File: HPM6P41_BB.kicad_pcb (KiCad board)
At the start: 4 copper layers, 152.8 x 80.3 mm, 287 parts, among them J1 USB_B, J10 Conn_01x01, J11 Conn_01x01, J12 Conn_01x01, J2 USB_C_Receptacle_USB2.0_16P, J3 Conn_02x16_Odd_Even, J4 Conn_ARM_JTAG_SWD_20, J5 Conn_01x03, J6 Conn_01x03, J7 SMA, J8 SMA, J9 Conn_01x01, Q1 HYG080N10LS1C2, Q2 HYG080N10LS1C2, Q3 HYG080N10LS1C2, Q4 HYG080N10LS1C2, Q5 S8050, SW1 焊盘, SW2 Push_Button, SW3 Push_Button, SW4 Push_Button, U1 UCC27211ADRMR, U10 TJA1044GTK/3Z, U11 TPS54302, U12 LP5907MFX-3.3, U13 REF3030, U14 LM5164DDA, U15 SY8089, U16 INA241A3xDDF, U17 INA241A3xDDF, U18 UCC27519, U19 XC6206PxxxMR, U2 UCC27211ADRMR, U20 SGM8551XN, U21 SGM8551XN, U22 TMP112xxDRL, U23 TPD4E05U06DQA, U3 UCC27519, U4 HPM6P41IPB1, U5 TPD4E05U06DQA, U6 AT24C08C-SSHM-T, U7 TMP112xxDRL, U8 TMP112xxDRL, U9 SIT3088ETK, Y1 24MHz ±10ppm 6pF

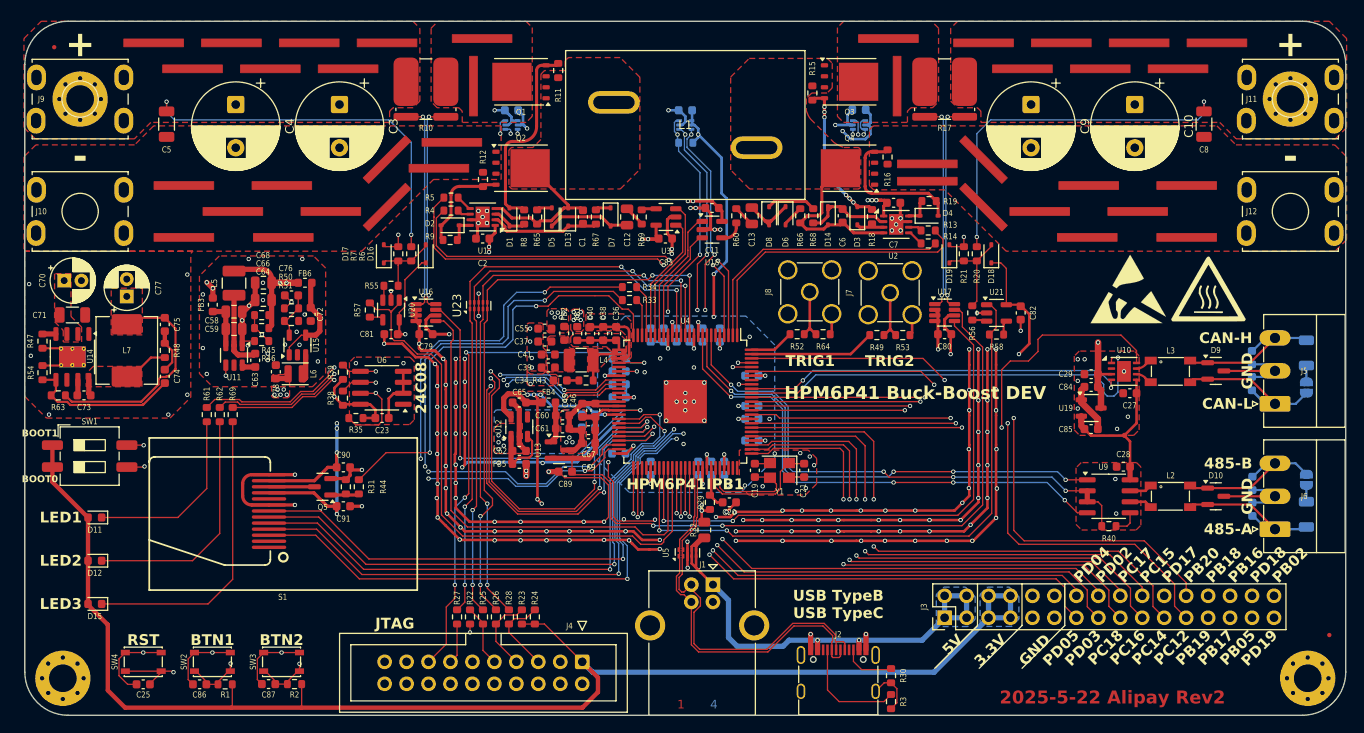
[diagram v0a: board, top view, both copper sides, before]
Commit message: 添加蜂鸣器IO及走线，更改PINMUX配图
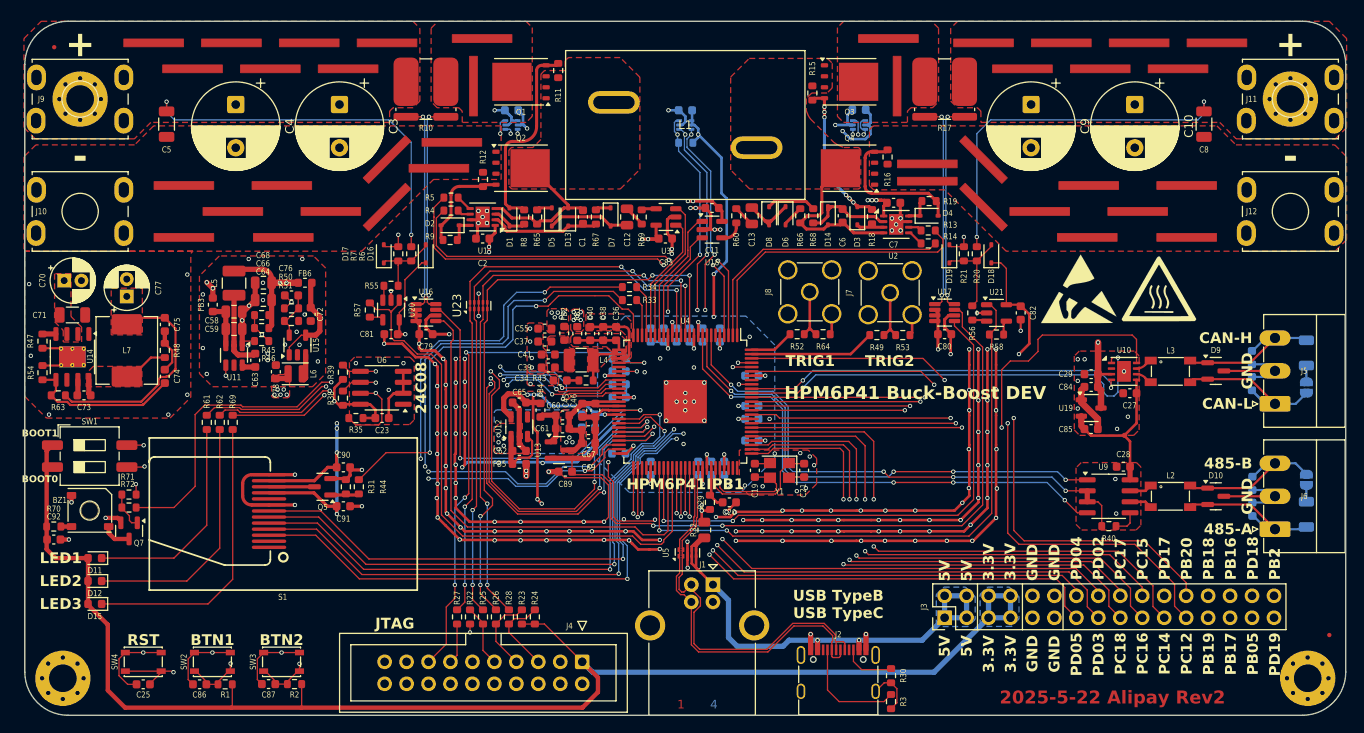
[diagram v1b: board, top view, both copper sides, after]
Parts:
- added BZ1: Buzzer_DummyPIn3, 1MyFootPrint:Buzzer_5020_MetalHole, F.Cu at (81.1, 94.6)
- added C92: 1uF, Capacitor_SMD:C_0603_1608Metric, F.Cu at (77.0, 98.0)
- added Q7: S8050, Package_TO_SOT_SMD:SOT-23, F.Cu at (85.7, 97.0)
- added R70: 0R, Resistor_SMD:R_0603_1608Metric, F.Cu at (77.0, 96.5)
- added R71: 4.7k, Resistor_SMD:R_0603_1608Metric, F.Cu at (85.7, 92.8)
- added R72: 100, Resistor_SMD:R_0603_1608Metric, F.Cu at (85.7, 94.2)
- moved G*** 5.73 mm to (204.8, 69.1)
- moved REF** 5.73 mm to (195.5, 68.9)
- moved D11 4.70 mm to (81.7, 100.1)
- moved D12 2.35 mm to (81.7, 102.8)
- moved FB4 1.30 mm to (133.2, 83.0), turned to -90 degrees
- moved R61 0.90 mm to (94.7, 84.4)
- moved R62 0.90 mm to (96.2, 84.4)
- moved R69 0.90 mm to (97.7, 84.4)
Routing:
- net /PY3: track 0.00 -> 71.2 mm, vias 0 -> 3
- net GND: track 599.5 -> 604.5 mm, vias 225 -> 229
- net Net-(Q7-B): track 0.00 -> 4.38 mm
- net Net-(D11-K): track 21.3 -> 24.8 mm
- net Net-(BZ1--): track 0.00 -> 3.40 mm
- net /PY0: track 54.3 -> 52.5 mm
- net /PY2: track 49.8 -> 48.1 mm
- net /PY1: track 52.1 -> 50.4 mm
- net Net-(BZ1-+): track 0.00 -> 1.22 mm
- net Net-(D12-K): track 27.9 -> 29.0 mm
- net Net-(D15-K): track 34.6 -> 33.7 mm
- net /PC13: track 56.0 -> 56.7 mm
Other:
- board text added: "PB2"
- board text removed: "PB02"

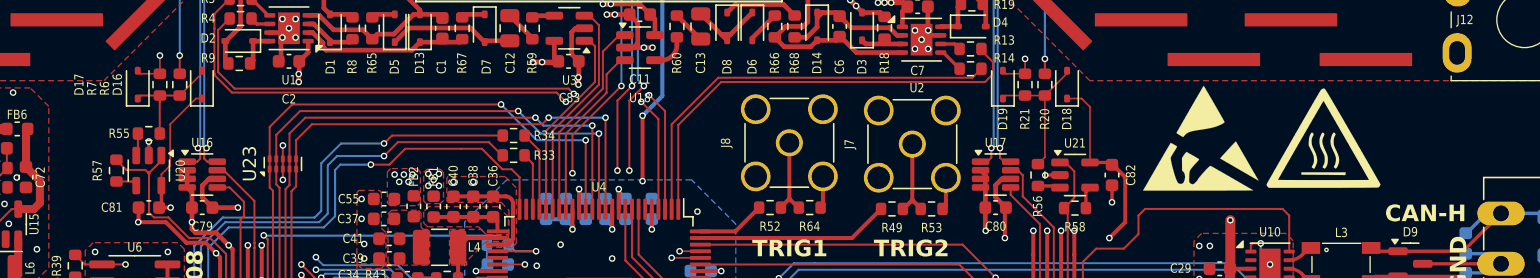
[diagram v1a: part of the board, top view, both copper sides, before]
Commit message: 修改丝印大小，位置
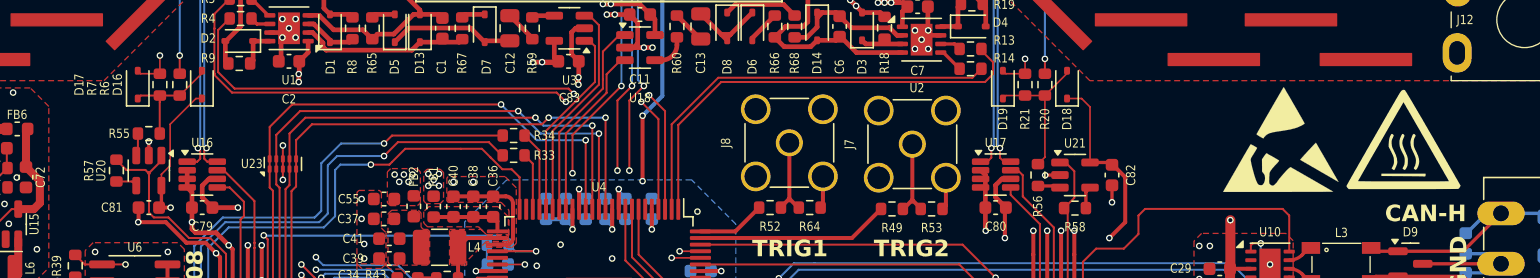
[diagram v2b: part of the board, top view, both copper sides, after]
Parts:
- moved G*** 6.05 mm to (210.8, 69.2)
- moved REF** 6.05 mm to (201.6, 69.0)
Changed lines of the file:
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@@
 		(tags "resistor")
 		(property "Reference" "R57"
-			(at 0 -1.43 90)
+			(at 0 -2.08 90)
 			(layer "F.SilkS")
 			(effects
@@
 		(locked yes)
 		(layer "F.Cu")
-		(at 204.774498 69.139757)
+		(at 210.824498 69.239757)
 		(property "Reference" "G***"
 			(at 0 0 0)
@@
 		(locked yes)
 		(layer "F.Cu")
-		(at 195.524498 68.929146)
+		(at 201.574498 69.029146)
 		(descr "Electrostatic discharge Logo")
 		(tags "Logo ESD")
@@
 		(tags "TSOT TO_SOT_SMD")
 		(property "Reference" "U20"
-			(at 0 -2.4 90)
+			(at 0 3.6125 90)
 			(layer "F.SilkS")
 			(effects
@@
 		(tags "USON-10 2.5x1.0mm Pitch 0.5mm")
 		(property "Reference" "U23"
-			(at 0.01829 -2.5 90)
+			(at 0.01829 -2.35 180)
 			(layer "F.SilkS")
 			(effects
 				(font
-					(size 1 1)
-					(thickness 0.15)
+					(size 0.7 0.6)
+					(thickness 0.1)
 				)
 			)

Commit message: no message
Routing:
- net +3.3V: track 375.8 -> 371.3 mm
- net /PA0: track 52.2 -> 50.7 mm
- net Net-(SW1-PIN3): track 75.6 -> 74.2 mm
- net GND: vias 229 -> 230
